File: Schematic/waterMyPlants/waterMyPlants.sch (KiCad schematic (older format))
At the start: 1 part

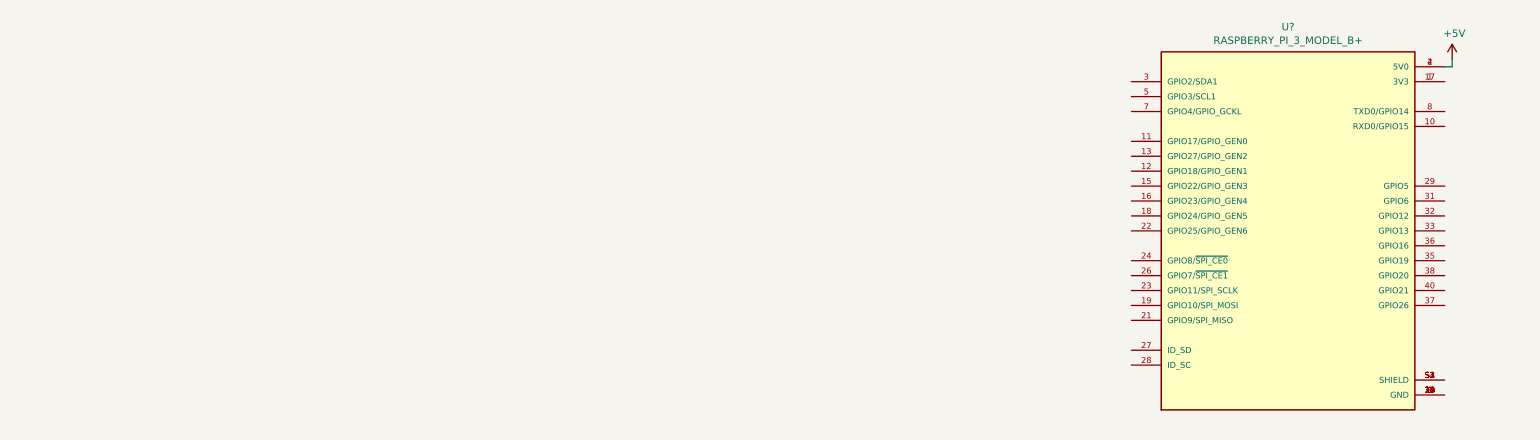
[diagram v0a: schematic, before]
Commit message: stream 1-3/27/2021
started the schematic and looked into detail what needed to be done to power the pi through solar panels/batteries
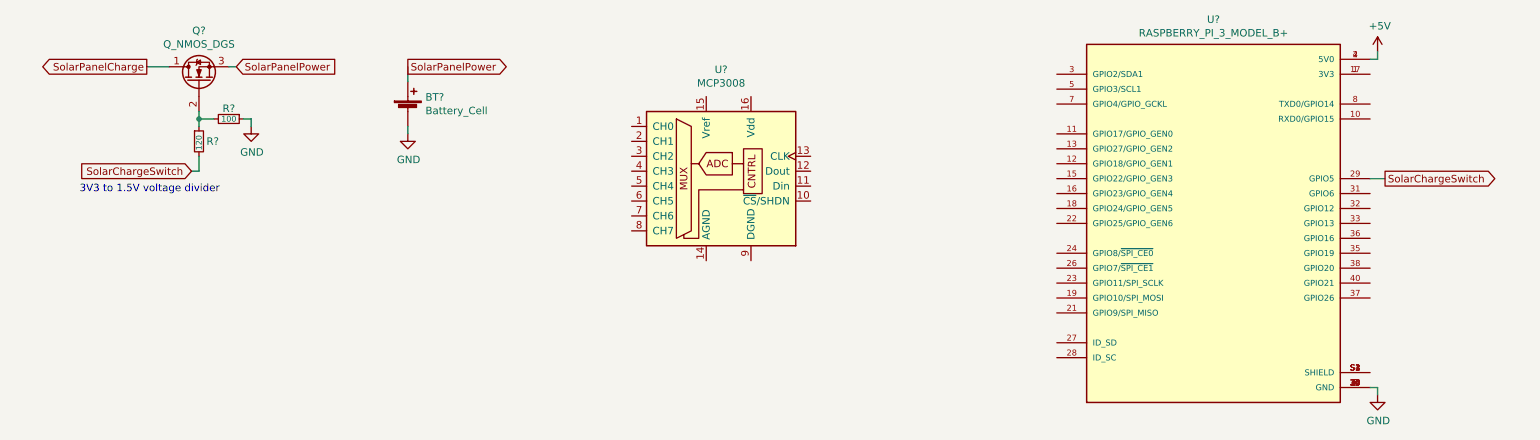
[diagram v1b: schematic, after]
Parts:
- removed U?: RASPBERRY_PI_3_MODEL_B+, MODULE_RASPBERRY_PI_3_MODEL_B+, symbol waterMyPlants:RASPBERRY_PI_3_MODEL_B+
- added BT?: Battery_Cell, symbol Device:Battery_Cell
- added Q?: Q_NMOS_DGS, symbol Device:Q_NMOS_DGS
- added R?: 120, symbol Device:R_Small
- added R?: 100, symbol Device:R_Small
- added U?: RASPBERRY_PI_3_MODEL_B+, MODULE_RASPBERRY_PI_3_MODEL_B+, symbol waterMyPlants:RASPBERRY_PI_3_MODEL_B+
- added U?: MCP3008, symbol Analog_ADC:MCP3008
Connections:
- net +5V: now also U?.2 (5V0), U?.4 (5V0)
- new net: U?.1 (3V3), U?.17 (3V3)
- new net: U?.S1 (SHIELD), U?.S2 (SHIELD), U?.S3 (SHIELD), U?.S4 (SHIELD)
- new net: Q?.2 (G), R?.1, R?.2
- new net GND: BT?.2 (-), R?.1, U?.14 (GND), U?.20 (GND), U?.25 (GND), U?.30 (GND), U?.34 (GND), U?.39 (GND), U?.6 (GND), U?.9 (GND)
- new net SolarChargeSwitch: R?.2, U?.29 (GPIO5)
- new net SolarPanelCharge: Q?.1 (D)
- new net SolarPanelPower: BT?.1 (+), Q?.3 (S)
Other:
- note added: "3V3 to 1.5V voltage divider"
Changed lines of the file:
@@
 L power:+5V #PWR?
 U 1 1 605FC4D5
-P 10150 850
-F 0 "#PWR?" H 10150 700 50  0001 C CNN
-F 1 "+5V" H 10165 1023 50  0000 C CNN
-F 2 "" H 10150 850 50  0001 C CNN
-F 3 "" H 10150 850 50  0001 C CNN
-	1    10150 850
+P 9650 800
+F 0 "#PWR?" H 9650 650 50  0001 C CNN
+F 1 "+5V" H 9665 973 50  0000 C CNN
+F 2 "" H 9650 800 50  0001 C CNN
+F 3 "" H 9650 800 50  0001 C CNN
+	1    9650 800
 	1    0    0    -1
 $EndComp
 Wire Wire Line
-	10100 900  10150 900
+	9600 850  9650 850
 Wire Wire Line
-	10150 900  10150 850
+	9650 850  9650 800
+$Comp
+L power:GND #PWR?
+U 1 1 605FEC65
+P 9650 3100
+F 0 "#PWR?" H 9650 2850 50  0001 C CNN
+F 1 "GND" H 9655 2927 50  0000 C CNN
+F 2 "" H 9650 3100 50  0001 C CNN
+F 3 "" H 9650 3100 50  0001 C CNN
+	1    9650 3100
+	1    0    0    -1
+$EndComp
+Wire Wire Line
+	9600 3050 9650 3050
+Wire Wire Line
+	9650 3050 9650 3100
 $Comp
 L waterMyPlants:RASPBERRY_PI_3_MODEL_B+ U?
-U 1 1 605FDDDC
-P 9100 1800
-F 0 "U?" H 9050 2967 50  0000 C CNN
-F 1 "RASPBERRY_PI_3_MODEL_B+" H 9050 2876 50  0000 C CNN
-F 2 "MODULE_RASPBERRY_PI_3_MODEL_B+" H 9100 1800 50  0001 L BNN
-F 3 "" H 9100 1800 50  0001 L BNN
-F 4 "Raspberry Pi" H 9100 1800 50  0001 L BNN "MF"
-F 5 "Raspberry Pi" H 9100 1800 50  0001 L BNN "Package"
-F 6 "RASPBERRY PI 3 MOD B+ BCM2837B0" H 9100 1800 50  0001 L BNN "Description"
-F 7 "None" H 9100 1800 50  0001 L BNN "Price"
-F 8 "https://pricing.snapeda.com/search/part/RASPBERRY PI 3 MODEL B+/?ref=eda" H 9100 1800 50  0001 L BNN "Purchase-URL"
-F 9 "RASPBERRY PI 3 MODEL B+" H 9100 1800 50  0001 L BNN "MP"
-F 10 "Warning" H 9100 1800 50  0001 L BNN "Availability"
-	1    9100 1800
+U 1 1 6060076F
+P 8600 1750
+F 0 "U?" H 8550 2917 50  0000 C CNN
+F 1 "RASPBERRY_PI_3_MODEL_B+" H 8550 2826 50  0000 C CNN
+F 2 "MODULE_RASPBERRY_PI_3_MODEL_B+" H 8600 1750 50  0001 L BNN
+F 3 "" H 8600 1750 50  0001 L BNN
+F 4 "Raspberry Pi" H 8600 1750 50  0001 L BNN "MF"
+F 5 "Raspberry Pi" H 8600 1750 50  0001 L BNN "Package"
+F 6 "RASPBERRY PI 3 MOD B+ BCM2837B0" H 8600 1750 50  0001 L BNN "Description"
+F 7 "None" H 8600 1750 50  0001 L BNN "Price"
+F 8 "https://pricing.snapeda.com/search/part/RASPBERRY PI 3 MODEL B+/?ref=eda" H 8600 1750 50  0001 L BNN "Purchase-URL"
+F 9 "RASPBERRY PI 3 MODEL B+" H 8600 1750 50  0001 L BNN "MP"
+F 10 "Warning" H 8600 1750 50  0001 L BNN "Availability"
+	1    8600 1750
 	1    0    0    -1
 $EndComp
+$Comp
+L Device:Q_NMOS_DGS Q?
+U 1 1 60604324
+P 1750 1000
+F 0 "Q?" V 2092 1000 50  0000 C CNN
+F 1 "Q_NMOS_DGS" V 2001 1000 50  0000 C CNN
+F 2 "" H 1950 1100 50  0001 C CNN
+F 3 "~" H 1750 1000 50  0001 C CNN
+	1    1750 1000
+	0    -1   -1   0
+$EndComp
+Text GLabel 9700 1650 2    50   Output ~ 0
+SolarChargeSwitch
+Wire Wire Line
+	9700 1650 9600 1650
+Text GLabel 1700 1600 0    50   Input ~ 0
+SolarChargeSwitch
+$Comp
+L Device:R_Small R?
+U 1 1 6060918F
+P 1750 1400
+F 0 "R?" H 1800 1400 50  0000 L CNN
+F 1 "120" V 1750 1340 39  0000 L CNN
+F 2 "" H 1750 1400 50  0001 C CNN
+F 3 "~" H 1750 1400 50  0001 C CNN
+	1    1750 1400
+	1    0    0    -1
+$EndComp
+$Comp
+L Device:R_Small R?
+U 1 1 6060B3F6
+P 1950 1250
+F 0 "R?" V 1880 1250 50  0000 C CNN
+F 1 "100" V 1950 1250 39  0000 C CNN
+F 2 "" H 1950 1250 50  0001 C CNN
+F 3 "~" H 1950 1250 50  0001 C CNN
+	1    1950 1250
+	0    1    1    0
+$EndComp
+Wire Wire Line
+	1700 1600 1750 1600
+Wire Wire Line
+	1750 1600 1750 1500
+Wire Wire Line
+	1750 1300 1750 1250
+Wire Wire Line
+	1850 1250 1750 1250
+Connection ~ 1750 1250
+Wire Wire Line
+	1750 1250 1750 1200
+$Comp
+L power:GND #PWR?
+U 1 1 6060D158
+P 2100 1300
+F 0 "#PWR?" H 2100 1050 50  0001 C CNN
+F 1 "GND" H 2105 1127 50  0000 C CNN
+F 2 "" H 2100 1300 50  0001 C CNN
+F 3 "" H 2100 1300 50  0001 C CNN
+	1    2100 1300
+	1    0    0    -1
+$EndComp
+Wire Wire Line
+	2050 1250 2100 1250
+Wire Wire Line
+	2100 1250 2100 1300
+Text Notes 950  1750 0    50   ~ 0
+3V3 to 1.5V voltage divider
+Text GLabel 2000 900  2    50   Input ~ 0
+SolarPanelPower
+Wire Wire Line
+	2000 900  1950 900
+Wire Wire Line
+	1550 900  1400 900
+Text GLabel 1400 900  0    50   Output ~ 0
+SolarPanelCharge
+$Comp
+L Device:Battery_Cell BT?
+U 1 1 60616C48
+P 3150 1200
+F 0 "BT?" H 3268 1296 50  0000 L CNN
+F 1 "Battery_Cell" H 3268 1205 50  0000 L CNN
+F 2 "" V 3150 1260 50  0001 C CNN
+F 3 "~" V 3150 1260 50  0001 C CNN
+	1    3150 1200
+	1    0    0    -1
+$EndComp
+Wire Wire Line
+	3150 900  3150 1000
+Text GLabel 3150 900  2    50   Output ~ 0
+SolarPanelPower
+$Comp
+L power:GND #PWR?
+U 1 1 60619708
+P 3150 1350
+F 0 "#PWR?" H 3150 1100 50  0001 C CNN
+F 1 "GND" H 3155 1177 50  0000 C CNN
+F 2 "" H 3150 1350 50  0001 C CNN
+F 3 "" H 3150 1350 50  0001 C CNN
+	1    3150 1350
+	1    0    0    -1
+$EndComp
+Wire Wire Line
+	3150 1300 3150 1350
+$Comp
+L Analog_ADC:MCP3008 U?
+U 1 1 6061C65F
+P 5250 1600
+F 0 "U?" H 5250 2281 50  0000 C CNN
+F 1 "MCP3008" H 5250 2190 50  0000 C CNN
+F 2 "" H 5350 1700 50  0001 C CNN
+F 3 "http://ww1.microchip.com/downloads/en/DeviceDoc/21295d.pdf" H 5350 1700 50  0001 C CNN
+	1    5250 1600
+	1    0    0    -1
+$EndComp
